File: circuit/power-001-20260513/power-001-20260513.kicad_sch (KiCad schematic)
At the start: 57 parts, among them J1 VIN, J2 +5V_{Line}, J3 Power, J4 Logic, J5 Sub_{Power}, J6 Sub_{Signal}, Q1 BSS138, Q2 PMOS, SW1 SW_SPDT, SW2 SW_SPDT, SW3 SW_SPDT, SW4 Locker_SW, U1 OKL-T/6-W12N-C, U2 OKL-T/6-W12N-C, U3 AZ1084-3.3, U4 BP5293-33, U5 PIC12F683-xSN

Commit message: Update 電源基板のバッテリー接続口のフットプリントを作成＆紐づけ
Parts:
- J1: footprint (none) -> @Thrive_footprint_power:Conn_01x02_Wire_Only
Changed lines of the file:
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@@
 			)
 		)
-		(property "Footprint" ""
+		(property "Footprint" "@Thrive_footprint_power:Conn_01x02_Wire_Only"
 			(at 22.86 30.48 0)
 			(hide yes)

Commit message: Update 電源基板のトグルスイッチのフットプリントを作成＆紐づけ
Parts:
- SW1, SW2, SW3: footprint (none) -> @Thrive_footprint_power:2MS1-T1-B4-M2-Q-E
- TP1, TP2, TP3, TP4, TP5: footprint (none) -> TestPoint:TestPoint_Loop_D1.80mm_Drill1.0mm_Beaded
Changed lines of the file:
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@@
 			)
 		)
-		(property "Footprint" ""
+		(property "Footprint" "TestPoint:TestPoint_Loop_D1.80mm_Drill1.0mm_Beaded"
 			(at 81.28 167.64 0)
 			(hide yes)
@@
 			)
 		)
-		(property "Footprint" ""
+		(property "Footprint" "TestPoint:TestPoint_Loop_D1.80mm_Drill1.0mm_Beaded"
 			(at 91.44 167.64 0)
 			(hide yes)
@@
 			)
 		)
-		(property "Footprint" ""
+		(property "Footprint" "TestPoint:TestPoint_Loop_D1.80mm_Drill1.0mm_Beaded"
 			(at 101.6 167.64 0)
 			(hide yes)
@@
 			)
 		)
-		(property "Footprint" ""
+		(property "Footprint" "TestPoint:TestPoint_Loop_D1.80mm_Drill1.0mm_Beaded"
 			(at 121.92 167.64 0)
 			(hide yes)
@@
 			)
 		)
-		(property "Footprint" ""
+		(property "Footprint" "TestPoint:TestPoint_Loop_D1.80mm_Drill1.0mm_Beaded"
 			(at 111.76 167.64 0)
 			(hide yes)
@@
 			)
 		)
-		(property "Footprint" ""
+		(property "Footprint" "@Thrive_footprint_power:2MS1-T1-B4-M2-Q-E"
 			(at 27.94 156.21 0)
 			(hide yes)
@@
 			)
 		)
-		(property "Footprint" ""
+		(property "Footprint" "@Thrive_footprint_power:2MS1-T1-B4-M2-Q-E"
 			(at 27.94 125.73 0)
 			(hide yes)
@@
 			)
 		)
-		(property "Footprint" ""
+		(property "Footprint" "@Thrive_footprint_power:2MS1-T1-B4-M2-Q-E"
 			(at 27.94 140.97 0)
 			(hide yes)

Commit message: Update コートヤード要件を追加した
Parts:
- F1: footprint (none) -> @Thrive_footprint_power:MF61NR_FUC-04
- SW4: footprint (none) -> @Thrive_footprint_power:DS-850K-S-ON-K
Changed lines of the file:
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@@
 			)
 		)
-		(property "Footprint" ""
+		(property "Footprint" "@Thrive_footprint_power:MF61NR_FUC-04"
 			(at 34.29 32.258 90)
 			(hide yes)
@@
 			)
 		)
-		(property "Footprint" ""
+		(property "Footprint" "@Thrive_footprint_power:DS-850K-S-ON-K"
 			(at 45.72 30.48 0)
 			(hide yes)

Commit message: Update ちょっと電源基板を修正
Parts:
- removed R20: 330, Resistor_SMD:R_0805_2012Metric, symbol Device:R_Small
- added J7: ICSP_{PIC12F683}, Connector_PinHeader_2.54mm:PinHeader_1x05_P2.54mm_Vertical, symbol Connector:Conn_01x05_Pin
- added R16: 330, Resistor_SMD:R_0805_2012Metric, symbol Device:R_Small
- added R21: 10k, Resistor_SMD:R_0805_2012Metric, symbol Device:R_Small
- D1: footprint Capacitor_SMD:C_0603_1608Metric -> LED_SMD:LED_0603_1608Metric
- renumbered R16 to R17, R17 to R18, R18 to R19, R19 to R20
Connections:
- net +3.3VA: now also J7.2 (Pin_2), R21.2
- net GND: now also J7.3 (Pin_3)
- net Prot-LED: now also U5.3 (GP4), R16.1; no longer U5.4 (GP3)
- net at D1.2 (A): now also R16.2
- net Prot-CTRL renamed ICSPCLK
- net ICSPCLK: now also J7.5 (Pin_5)
- net Prot-Vraw renamed ICSPDAT
- net ICSPDAT: now also J7.4 (Pin_4)
- new net MCLR: J7.1 (Pin_1), R21.1, U5.4 (GP3)
- no-connect marks 2 -> 1
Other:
- moved on the sheet: BZ1, Q1, Q2, R17, R18, R19, R20

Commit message: Update 電源基板の配置が苦しい
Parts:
- removed C5: 1000μ, Capacitor_THT:CP_Radial_D10.0mm_P5.00mm, symbol Device:C
- removed D1: LED, LED_SMD:LED_0603_1608Metric, symbol Device:LED_Small
- removed R16: 330, Resistor_SMD:R_0805_2012Metric, symbol Device:R_Small
- removed TP1, TP2: TP_{+5V-Line}, TestPoint:TestPoint_Loop_D1.80mm_Drill1.0mm_Beaded, symbol Connector:TestPoint_Small
- removed TP3: TP_{+5V}, TestPoint:TestPoint_Loop_D1.80mm_Drill1.0mm_Beaded, symbol Connector:TestPoint_Small
- removed TP4: TP_{+3.3V}, TestPoint:TestPoint_Loop_D1.80mm_Drill1.0mm_Beaded, symbol Connector:TestPoint_Small
- removed TP5: TP_{GND}, TestPoint:TestPoint_Loop_D1.80mm_Drill1.0mm_Beaded, symbol Connector:TestPoint_Small
- removed U4: BP5293-33, @Thrive_footprint_power:BP5293-33, symbol @Thrive_symbol_power:BP5293-33
- added C13, C5: 10μ, Capacitor_SMD:C_0805_2012Metric, symbol Device:C_Small
- added U6: LM1117MP-3.3, Package_TO_SOT_SMD:SOT-223-3_TabPin2, symbol Regulator_Linear:LM1117MP-3.3
- J2, J3, J4, J5: footprint Connector_AMASS:AMASS_XT30PW-F_1x02_P2.50mm_Horizontal -> @Thrive_footprint_power:AMASS_XT30PW-F_1x02_P2.50mm_Horizontal
- J7: footprint Connector_PinHeader_2.54mm:PinHeader_1x05_P2.54mm_Vertical -> Connector_PinHeader_1.00mm:PinHeader_1x05_P1.00mm_Vertical
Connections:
- net +3.3VA: now also C13.1, U6.2 (VO)
- net GND: now also C13.2, C5.2, U6.1 (GND)
- net VCC: now also C5.1, U6.3 (VI)
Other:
- moved on the sheet: BZ1, C1, C12, J7, Q1, Q2, R17, R18, R19, R20, R21, U5

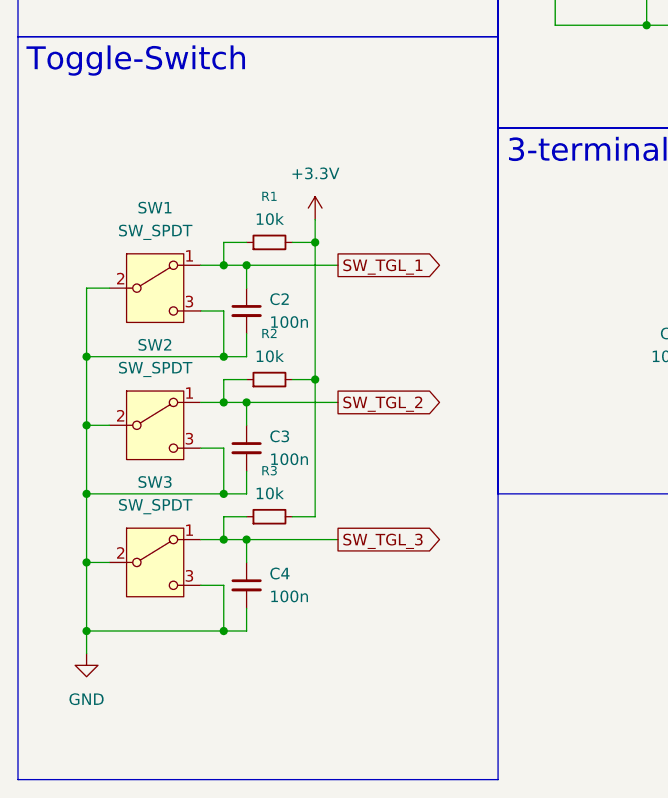
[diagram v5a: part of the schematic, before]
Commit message: Update 電源基板の回路図とPCBを修正・更新
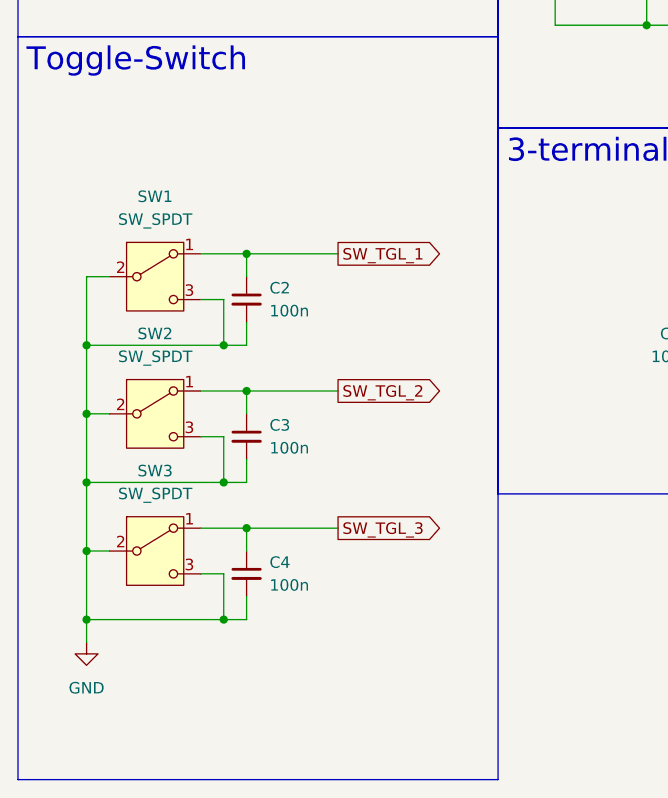
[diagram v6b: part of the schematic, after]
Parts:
- removed R1, R2, R3: 10k, Resistor_SMD:R_0805_2012Metric, symbol Device:R_Small
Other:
- moved on the sheet: C2, C3, C4, SW1, SW2, SW3

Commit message: Update 電源基板のボード図作成終わり！！！！
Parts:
- added J8: ESC, @Thrive_footprint_power:Conn_01x02_Wire_Only_SMD, symbol Connector:Conn_01x02_Pin
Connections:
- net GND: now also J8.2 (Pin_2)
- net VIN: now also J8.1 (Pin_1)
- net Prot-LED: no longer names the net of U5.3 (GP4)
- no-connect marks 1 -> 2
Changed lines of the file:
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@@
 		)
 	)
+	(text_box "Voltage-OUT_{ESC}"
+		(exclude_from_sim no)
+		(at 66.04 148.59 0)
+		(size 44.45 31.75)
+		(margins 0.9525 0.9525 0.9525 0.9525)
+		(stroke
+			(width 0)
+			(type solid)
+		)
+		(fill
+			(type none)
+		)
+		(effects
+			(font
+				(size 2.54 2.54)
+			)
+			(justify left top)
+		)
+	)
 	(text_box "Protection-Circuit"
 		(exclude_from_sim no)
@@
 		(at 222.25 41.91)
 	)
+	(no_connect
+		(at 222.25 39.37)
+	)
 	(wire
 		(pts
@@
 	(wire
 		(pts
+			(xy 90.17 165.1) (xy 87.63 165.1)
+		)
+		(stroke
+			(width 0)
+			(type default)
+		)
+	)
+	(wire
+		(pts
 			(xy 120.65 45.72) (xy 123.19 45.72)
 		)
@@
 	(wire
 		(pts
-			(xy 222.25 39.37) (xy 224.79 39.37)
+			(xy 175.26 68.58) (xy 177.8 68.58)
 		)
 		(stroke
@@
 	(wire
 		(pts
-			(xy 175.26 68.58) (xy 177.8 68.58)
+			(xy 35.56 132.08) (xy 38.1 132.08)
 		)
 		(stroke
@@
 	(wire
 		(pts
-			(xy 35.56 132.08) (xy 38.1 132.08)
+			(xy 172.72 76.2) (xy 175.26 76.2)
 		)
 		(stroke
@@
 	(wire
 		(pts
-			(xy 172.72 76.2) (xy 175.26 76.2)
+			(xy 182.88 119.38) (xy 180.34 119.38)
 		)
 		(stroke
@@
 	(wire
 		(pts
-			(xy 182.88 119.38) (xy 180.34 119.38)
+			(xy 102.87 43.18) (xy 102.87 45.72)
 		)
 		(stroke
@@
 	(wire
 		(pts
-			(xy 102.87 43.18) (xy 102.87 45.72)
+			(xy 118.11 43.18) (xy 118.11 36.83)
 		)
 		(stroke
@@
 	(wire
 		(pts
-			(xy 118.11 43.18) (xy 118.11 36.83)
+			(xy 245.11 24.13) (xy 247.65 24.13)
 		)
 		(stroke
@@
 	(wire
 		(pts
-			(xy 245.11 24.13) (xy 247.65 24.13)
+			(xy 90.17 162.56) (xy 90.17 165.1)
 		)
 		(stroke
@@
 	(wire
 		(pts
+			(xy 90.17 170.18) (xy 90.17 167.64)
+		)
+		(stroke
+			(width 0)
+			(type default)
+		)
+	)
+	(wire
+		(pts
 			(xy 207.01 21.59) (xy 207.01 24.13)
 		)
@@
 	(wire
 		(pts
+			(xy 90.17 167.64) (xy 87.63 167.64)
+		)
+		(stroke
+			(width 0)
+			(type default)
+		)
+	)
+	(wire
+		(pts
 			(xy 72.39 26.67) (xy 72.39 29.21)
 		)
@@
 		)
 	)
-	(global_label "Prot-LED"
-		(shape output)
-		(at 224.79 39.37 0)
-		(fields_autoplaced yes)
-		(effects
-			(font
-				(size 1.27 1.27)
-			)
-			(justify left)
-		)
-		(property "Intersheetrefs" "${INTERSHEET_REFS}"
-			(at 236.0693 39.37 0)
-			(hide yes)
-			(show_name no)
-			(do_not_autoplace no)
-			(effects
-				(font
-					(size 1.27 1.27)
-				)
-				(justify left)
-			)
-		)
-	)
 	(global_label "Prot-CTRL"
 		(shape input)
@@
 		)
 	)
+	(global_label "VIN"
+		(shape input)
+		(at 90.17 162.56 90)
+		(fields_autoplaced yes)
+		(effects
+			(font
+				(size 1.27 1.27)
+			)
+			(justify left)
+		)
+		(property "Intersheetrefs" "${INTERSHEET_REFS}"
+			(at 90.17 156.2437 90)
+			(hide yes)
+			(show_name no)
+			(do_not_autoplace no)
+			(effects
+				(font
+					(size 1.27 1.27)
+				)
+				(justify left)
+			)
+		)
+	)
 	(global_label "Prot-Buzzer"
 		(shape input)
@@
 	)
 	(symbol
+		(lib_id "Connector:Conn_01x02_Pin")
+		(at 82.55 165.1 0)
+		(unit 1)
+		(body_style 1)
+		(exclude_from_sim no)
+		(in_bom yes)
+		(on_board yes)
+		(in_pos_files yes)
+		(dnp no)
+		(fields_autoplaced yes)
+		(property "Reference" "J8"
+			(at 83.185 160.02 0)
+			(show_name no)
+			(do_not_autoplace no)
+			(effects
+				(font
+					(size 1.27 1.27)
+				)
+			)
+		)
+		(property "Value" "ESC"
+			(at 83.185 162.56 0)
+			(show_name no)
+			(do_not_autoplace no)
+			(effects
+				(font
+					(size 1.27 1.27)
+				)
+			)
+		)
+		(property "Footprint" "@Thrive_footprint_power:Conn_01x02_Wire_Only_SMD"
+			(at 82.55 165.1 0)
+			(hide yes)
+			(show_name no)
+			(do_not_autoplace no)
+			(effects
+				(font
+					(size 1.27 1.27)
+				)
+			)
+		)
+		(property "Datasheet" ""
+			(at 82.55 165.1 0)
+			(hide yes)
+			(show_name no)
+			(do_not_autoplace no)
+			(effects
+				(font
+					(size 1.27 1.27)
+				)
+			)
+		)
+		(property "Description" "Generic connector, single row, 01x02, script generated"
+			(at 82.55 165.1 0)
+			(hide yes)
+			(show_name no)
+			(do_not_autoplace no)
+			(effects
+				(font
+					(size 1.27 1.27)
+				)
+			)
+		)
+		(pin "1"
+		)
+		(pin "2"
+		)
+		(instances
+			(project "power-001-20260513"
+				(path "/d54cd6d9-a65b-4f01-a2a7-b95d40372036"
+					(reference "J8")
+					(unit 1)
+				)
+			)
+		)
+	)
+	(symbol
 		(lib_id "Device:C_Small")
 		(at 72.39 39.37 0)
@@
 					(unit 1)
 				)
+			)
+		)
+	)
+	(symbol
+		(lib_id "power:GND")
+		(at 90.17 170.18 0)
+		(unit 1)
+		(body_style 1)
+		(exclude_from_sim no)
+		(in_bom yes)
+		(on_board yes)
+		(in_pos_files yes)
+		(dnp no)
+		(fields_autoplaced yes)
+		(property "Reference" "#PWR04"
+			(at 90.17 176.53 0)
+			(hide yes)
+			(show_name no)
+			(do_not_autoplace no)
+			(effects
+				(font
+					(size 1.27 1.27)
+				)
+			)
+		)
+		(property "Value" "GND"
+			(at 90.17 175.26 0)
+			(show_name no)
+			(do_not_autoplace no)
+			(effects
+				(font
+					(size 1.27 1.27)
+				)
+			)
+		)
+		(property "Footprint" ""
+			(at 90.17 170.18 0)
+			(hide yes)
+			(show_name no)
+			(do_not_autoplace no)
+			(effects
+				(font
+					(size 1.27 1.27)
+				)
+			)
+		)
+		(property "Datasheet" ""
+			(at 90.17 170.18 0)
+			(hide yes)
+			(show_name no)
+			(do_not_autoplace no)
+			(effects
+				(font
+					(size 1.27 1.27)
+				)
+			)
+		)
+		(property "Description" "Power symbol creates a global label with name \"GND\" , ground"
+			(at 90.17 170.18 0)
+			(hide yes)
+			(show_name no)
+			(do_not_autoplace no)
+			(effects
+				(font
+					(size 1.27 1.27)
+				)
+			)
+		)
+		(pin "1"
+		)
+		(instances
+			(project "power-001-20260513"
+				(path "/d54cd6d9-a65b-4f01-a2a7-b95d40372036"
+					(reference "#PWR04")
+					(unit 1)
+				)

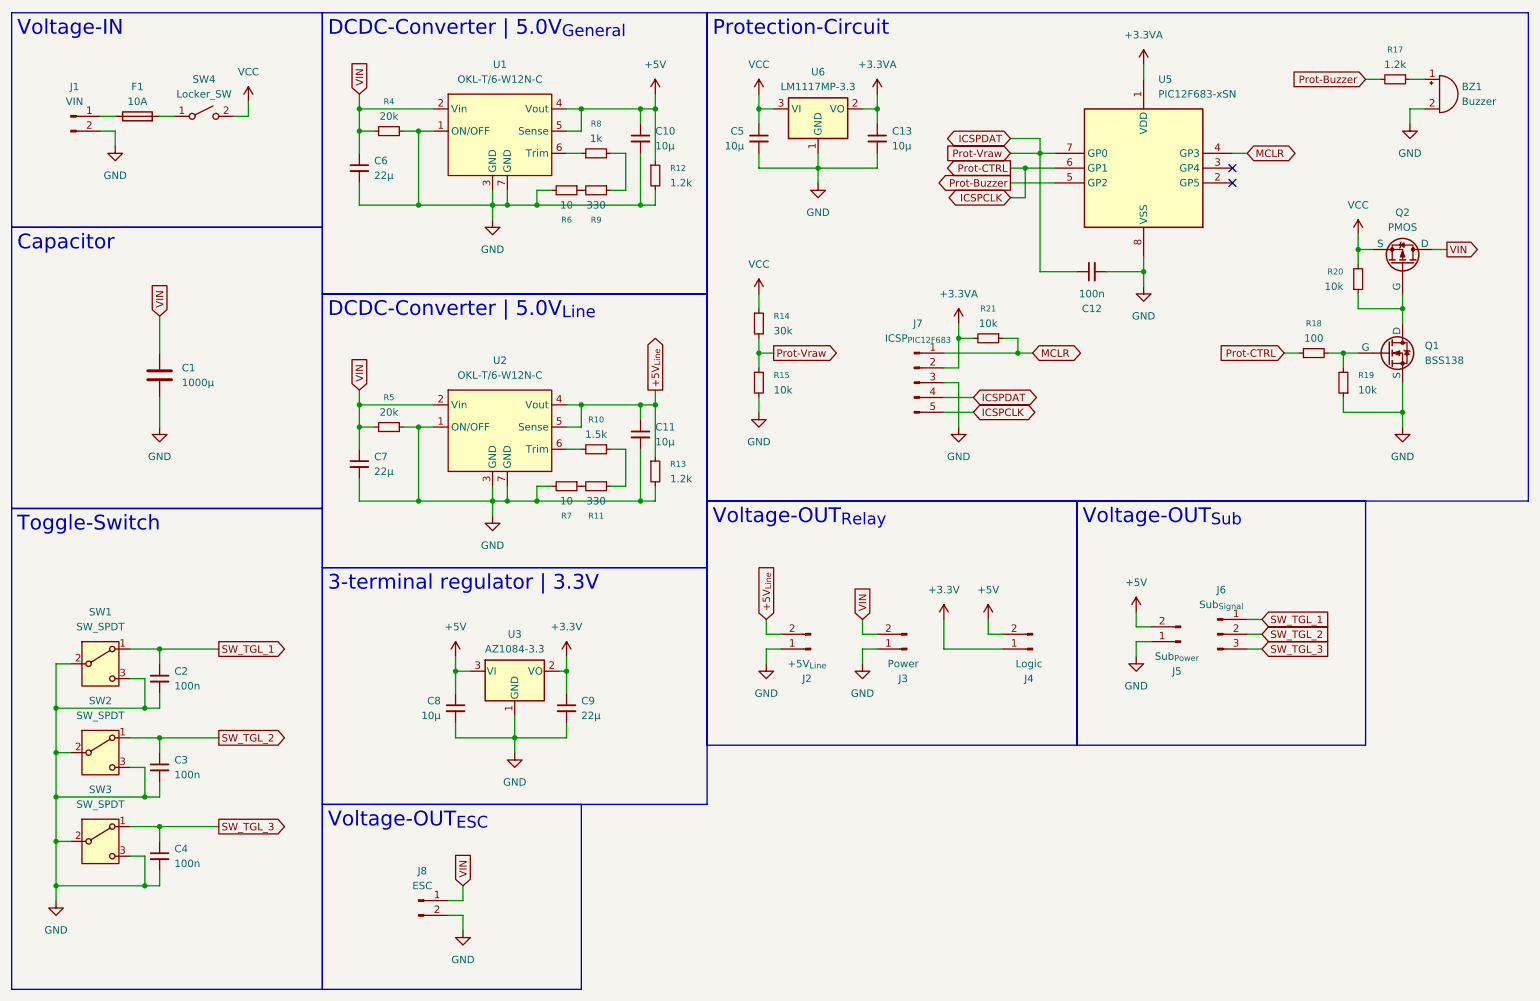
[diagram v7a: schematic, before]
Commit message: Update 電源基板いったん完成、シルクスクリーンだけきれいにしなきゃ
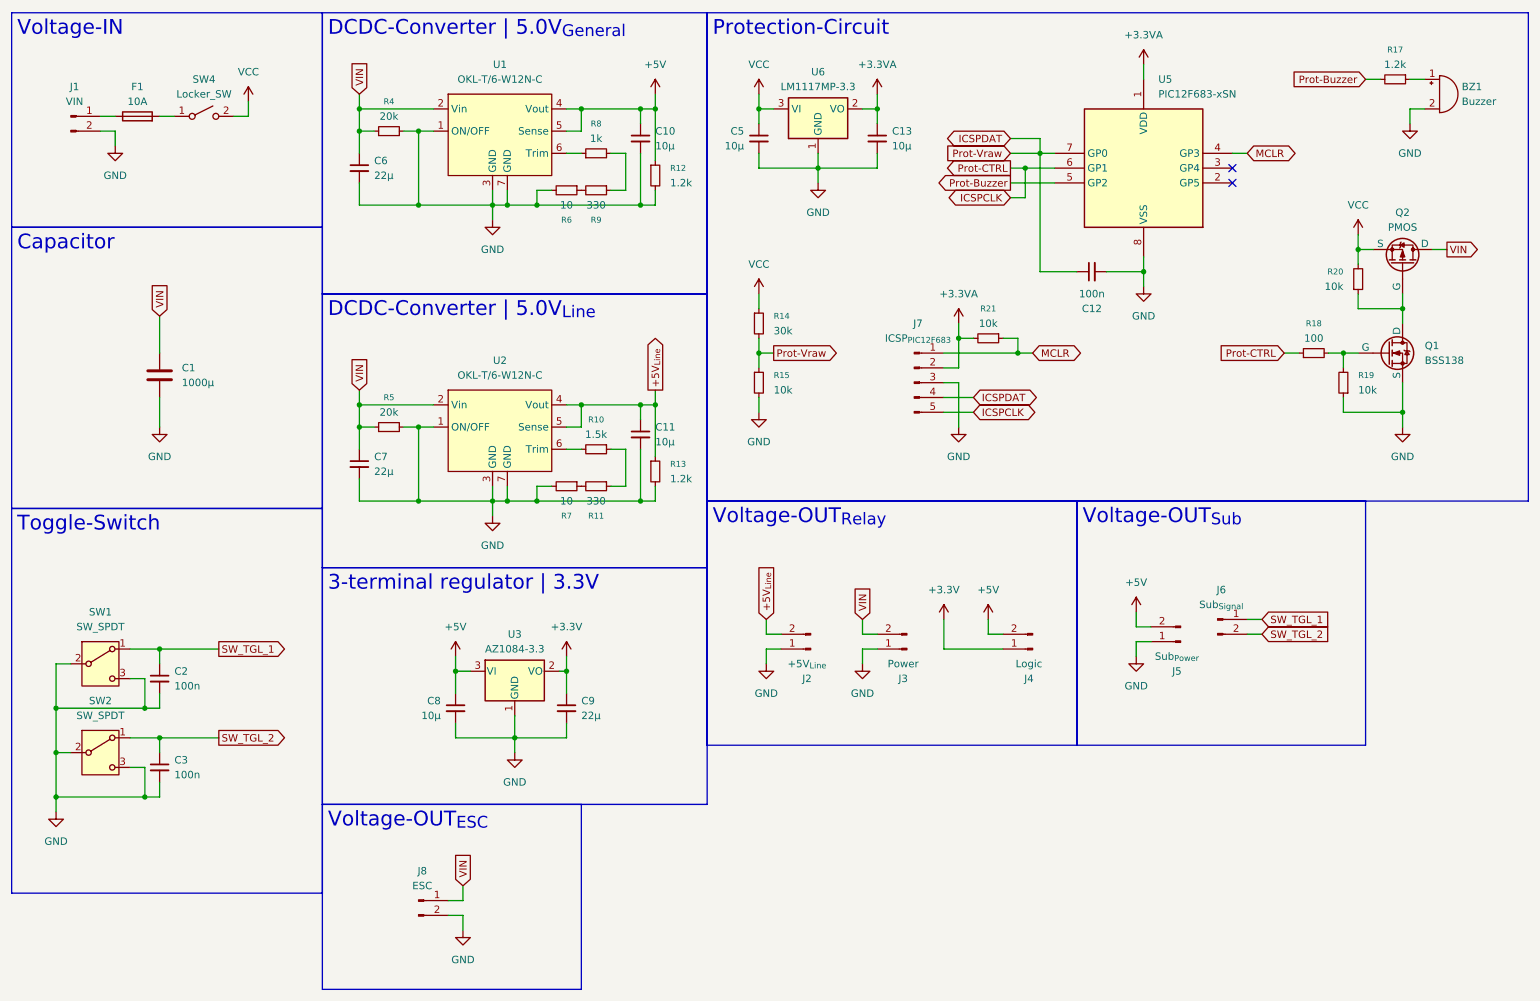
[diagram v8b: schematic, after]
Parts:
- removed C4: 100n, Capacitor_SMD:C_0805_2012Metric, symbol Device:C_Small
- removed J6: Sub_{Signal}, Connector_PinHeader_2.54mm:PinHeader_1x03_P2.54mm_Horizontal, symbol Connector:Conn_01x03_Pin
- removed SW3: SW_SPDT, @Thrive_footprint_power:2MS1-T1-B4-M2-Q-E, symbol Switch:SW_SPDT
- added J6: Sub_{Signal}, Connector_PinHeader_2.54mm:PinHeader_1x02_P2.54mm_Horizontal, symbol Connector:Conn_01x02_Pin
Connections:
- net SW_TGL_1: now also J6.1 (Pin_1)
- net SW_TGL_2: now also J6.2 (Pin_2)
